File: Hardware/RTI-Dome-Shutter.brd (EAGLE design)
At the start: 80 x 71.1 mm, 42 parts, among them IC1 24AA128ST, IC5 74LVC245, IC6 74ABT245, J1 POWERPOLE_POWER45A

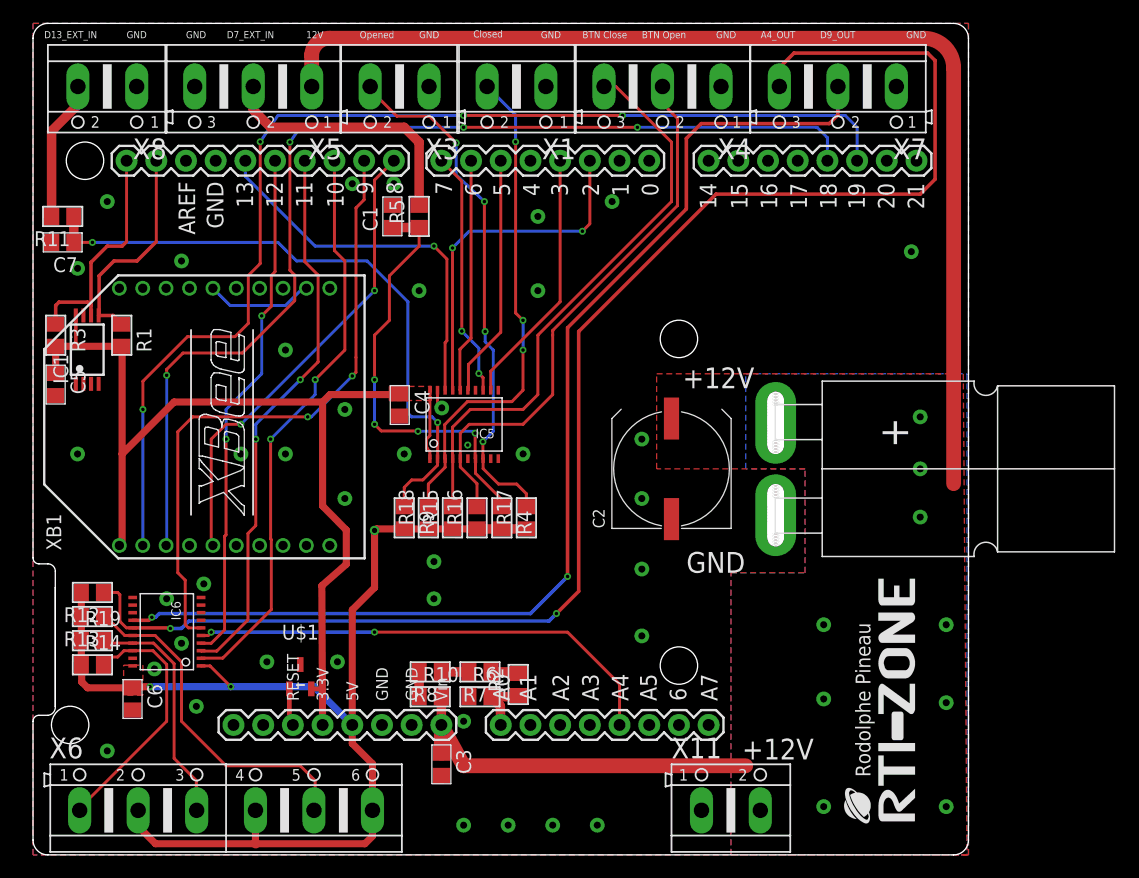
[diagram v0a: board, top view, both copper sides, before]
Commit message: Change pin mode for better interrupt detection
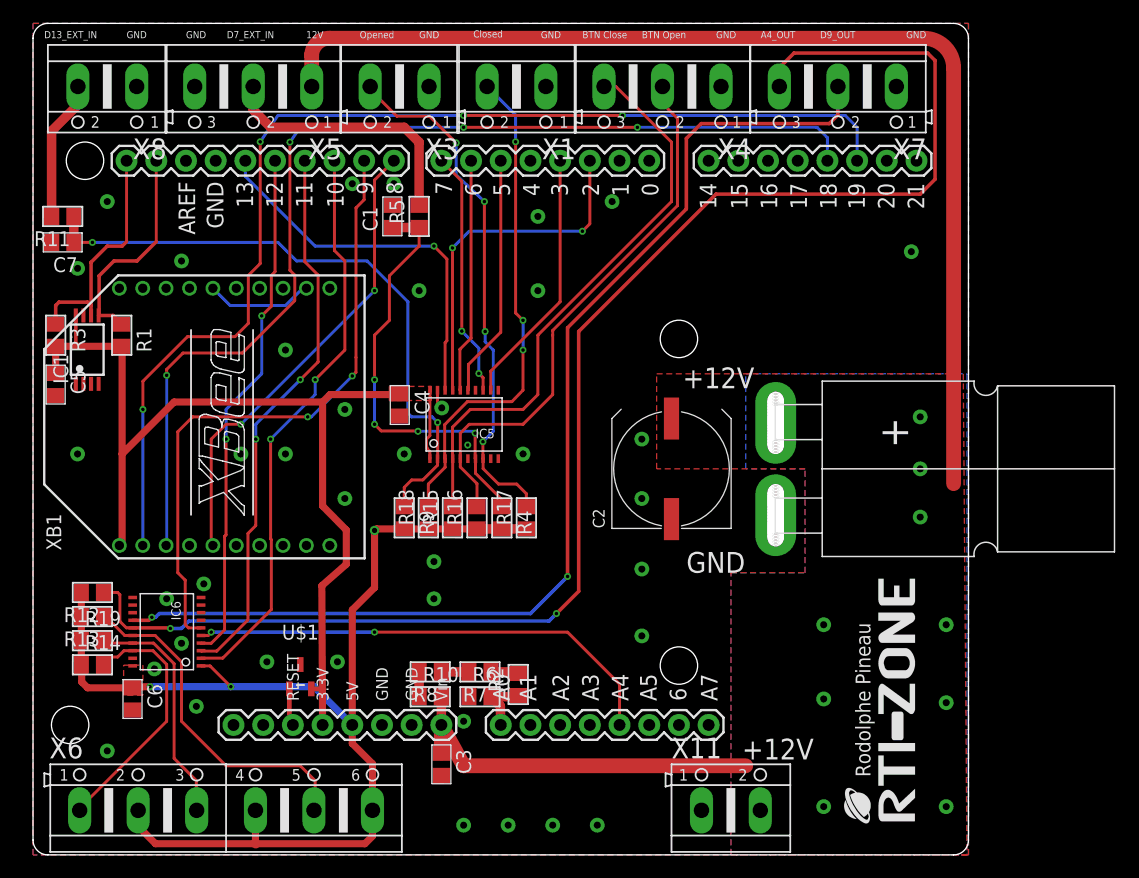
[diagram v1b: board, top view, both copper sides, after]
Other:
- outline, holes or cut-outs redrawn
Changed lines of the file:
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@@
 <setting verticaltext="up"/>
 </settings>
-<grid distance="0.3175" unitdist="mm" unit="mm" style="lines" multiple="1" display="yes" altdistance="0.03175" altunitdist="mm" altunit="mm"/>
+<grid distance="0.635" unitdist="mm" unit="mm" style="lines" multiple="1" display="yes" altdistance="0.03175" altunitdist="mm" altunit="mm"/>
 <layers>
 <layer number="1" name="Top" color="4" fill="1" visible="yes" active="yes"/>
@@
 <text x="55.88" y="24.13" size="1.778" layer="21">GND</text>
 <text x="55.5625" y="39.90975" size="1.778" layer="21">+12V</text>
-<wire x1="1.905" y1="22.86" x2="1.905" y2="12.7" width="0" layer="20"/>
 <text x="37.6555" y="69.9135" size="0.6096" layer="21">Closed</text>
 <text x="27.94" y="69.85" size="0.6096" layer="21">Opened</text>
-<wire x1="0.508" y1="11.938" x2="1.27" y2="11.938" width="0" layer="20"/>
-<wire x1="0" y1="1.27" x2="0" y2="11.43" width="0" layer="20"/>
-<wire x1="1.905" y1="12.7" x2="1.905" y2="22.86" width="0" layer="20"/>
-<wire x1="0" y1="25.4" x2="0" y2="69.85" width="0" layer="20"/>
-<wire x1="1.27" y1="71.12" x2="78.74" y2="71.12" width="0" layer="20"/>
-<wire x1="80.01" y1="69.85" x2="80.01" y2="1.27" width="0" layer="20"/>
-<wire x1="78.74" y1="0" x2="1.27" y2="0" width="0" layer="20"/>
-<wire x1="1.905" y1="12.7" x2="1.27" y2="11.938" width="0" layer="20" curve="-90"/>
-<wire x1="78.74" y1="0" x2="80.01" y2="1.27" width="0" layer="20" curve="90"/>
-<wire x1="80.01" y1="69.85" x2="78.74" y2="71.12" width="0" layer="20" curve="90"/>
-<wire x1="1.27" y1="71.12" x2="0" y2="69.85" width="0" layer="20" curve="90"/>
-<wire x1="1.27" y1="0" x2="0" y2="1.27" width="0" layer="20" curve="-90"/>
-<wire x1="1.905" y1="24.257" x2="1.905" y2="22.86" width="0" layer="20"/>
-<wire x1="0.508" y1="24.892" x2="1.27" y2="24.892" width="0" layer="20"/>
-<wire x1="1.27" y1="24.892" x2="1.905" y2="24.257" width="0" layer="20" curve="-90"/>
-<wire x1="0.508" y1="24.892" x2="0" y2="25.4" width="0" layer="20" curve="-90"/>
-<wire x1="0" y1="11.43" x2="0.508" y2="11.938" width="0" layer="20" curve="-90"/>
 <text x="16.5735" y="69.85" size="0.6096" layer="21">D7_EXT_IN</text>
 <text x="13.081" y="69.85" size="0.6096" layer="21">GND</text>
@@
 <text x="60.6425" y="8.15975" size="1.778" layer="21">+12V</text>
 <text x="62.23" y="69.85" size="0.6096" layer="21">A4_OUT</text>
+<wire x1="0" y1="1.27" x2="0" y2="69.85" width="0" layer="20"/>
+<wire x1="0" y1="69.85" x2="1.27" y2="71.12" width="0" layer="20" curve="-90"/>
+<wire x1="1.27" y1="71.12" x2="78.74" y2="71.12" width="0" layer="20"/>
+<wire x1="78.74" y1="71.12" x2="80.01" y2="69.85" width="0" layer="20" curve="-90"/>
+<wire x1="80.01" y1="69.85" x2="80.01" y2="1.27" width="0" layer="20"/>
+<wire x1="80.01" y1="1.27" x2="78.74" y2="0" width="0" layer="20" curve="-90"/>
+<wire x1="78.74" y1="0" x2="1.27" y2="0" width="0" layer="20"/>
+<wire x1="1.27" y1="0" x2="0" y2="1.27" width="0" layer="20" curve="-90"/>
 </plain>
 <attributes>

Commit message: All recent update to pcb and code are in.
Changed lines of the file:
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@@
 <text x="0.9525" y="69.85" size="0.6096" layer="21">D13_EXT_IN</text>
 <text x="6.50875" y="68.61175" size="0.6096" layer="22" rot="MR0">D13_EXT_IN</text>
-<text x="34.925" y="3.4925" size="1.778" layer="51">Dome Shutter</text>
+<text x="34.925" y="3.4925" size="1.778" layer="25">Dome Shutter</text>
 <text x="60.6425" y="8.15975" size="1.778" layer="21">+12V</text>
 <text x="62.23" y="69.85" size="0.6096" layer="21">A4_OUT</text>

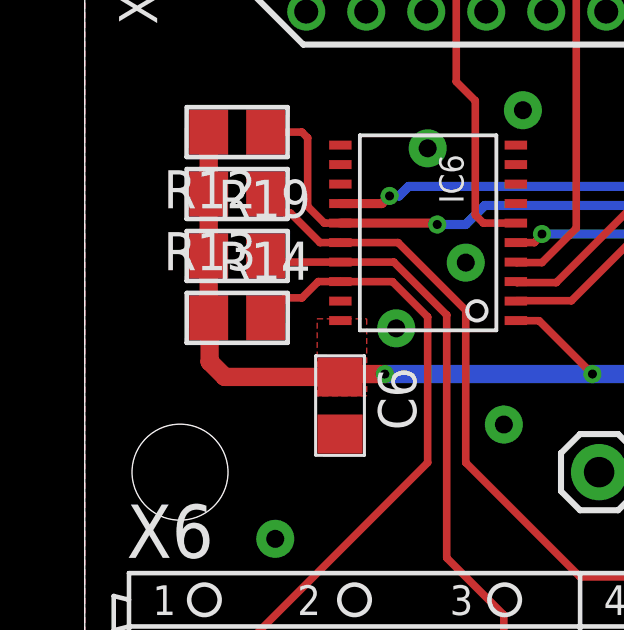
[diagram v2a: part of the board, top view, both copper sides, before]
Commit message: Re-did some of the core to receive data from network and wireless connection
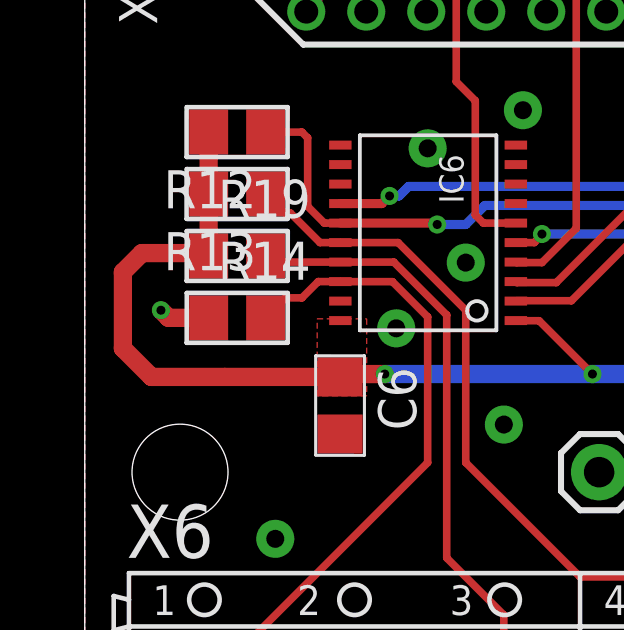
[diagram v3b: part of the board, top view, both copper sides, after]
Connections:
- net GND: now also R14.1
- net VCC: no longer R14.1
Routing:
- net VCC: track 102.0 -> 107.2 mm
- net GND: track 1.66 -> 3.36 mm, vias 39 -> 40
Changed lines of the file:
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@@
 <via x="12.7" y="18.0975" extent="1-16" drill="0.6" diameter="1.27"/>
 <contactref element="IC5" pad="P$9"/>
+<contactref element="R14" pad="1"/>
+<wire x1="4.13" y1="16.256" x2="2.794" y2="16.256" width="0.6096" layer="1"/>
+<wire x1="2.794" y1="16.256" x2="2.54" y2="16.51" width="0.6096" layer="1"/>
+<via x="2.54" y="16.51" extent="1-16" drill="0.3"/>
 </signal>
 <signal name="+12V" class="1">
@@
 <contactref element="R15" pad="1"/>
 <contactref element="R16" pad="1"/>
-<contactref element="R14" pad="1"/>
 <contactref element="R19" pad="1"/>
 <contactref element="R4" pad="2"/>
@@
 <wire x1="19.0246" y1="3.81" x2="19.0246" y2="0.9779" width="0.6096" layer="1"/>
 <wire x1="19.0246" y1="0.9779" x2="19.05" y2="0.9525" width="0.8128" layer="1"/>
-<wire x1="4.16175" y1="14.793" x2="4.66725" y2="14.2875" width="0.6096" layer="1"/>
 <wire x1="4.66725" y1="14.2875" x2="8.5065" y2="14.2875" width="0.6096" layer="1"/>
 <wire x1="8.5065" y1="14.2875" x2="8.509" y2="14.285" width="0.8128" layer="1"/>
 <contactref element="IC6" pad="P$20"/>
-<wire x1="4.16175" y1="14.793" x2="4.16175" y2="16.22425" width="0.6096" layer="1"/>
-<wire x1="4.16175" y1="16.22425" x2="4.13" y2="16.256" width="0.6096" layer="1"/>
-<wire x1="4.13" y1="16.256" x2="4.13" y2="18.31975" width="0.6096" layer="1"/>
 <wire x1="4.13" y1="20.3835" x2="3.8735" y2="20.3835" width="0.6096" layer="1"/>
 <wire x1="3.8735" y1="20.3835" x2="3.81" y2="20.32" width="0.6096" layer="1"/>
@@
 <wire x1="16.92275" y1="14.38275" x2="24.03475" y2="14.38275" width="0.6096" layer="16"/>
 <wire x1="24.03475" y1="14.38275" x2="27.305" y2="11.1125" width="0.6096" layer="16"/>
+<wire x1="4.66725" y1="14.2875" x2="2.2225" y2="14.2875" width="0.6096" layer="1"/>
+<wire x1="2.2225" y1="14.2875" x2="1.27" y2="15.24" width="0.6096" layer="1"/>
+<wire x1="1.27" y1="15.24" x2="1.27" y2="17.78" width="0.6096" layer="1"/>
+<wire x1="1.27" y1="17.78" x2="1.905" y2="18.415" width="0.6096" layer="1"/>
+<wire x1="1.905" y1="18.415" x2="4.03475" y2="18.415" width="0.6096" layer="1"/>
+<wire x1="4.03475" y1="18.415" x2="4.13" y2="18.31975" width="0.6096" layer="1"/>
 </signal>
 <signal name="N$2">

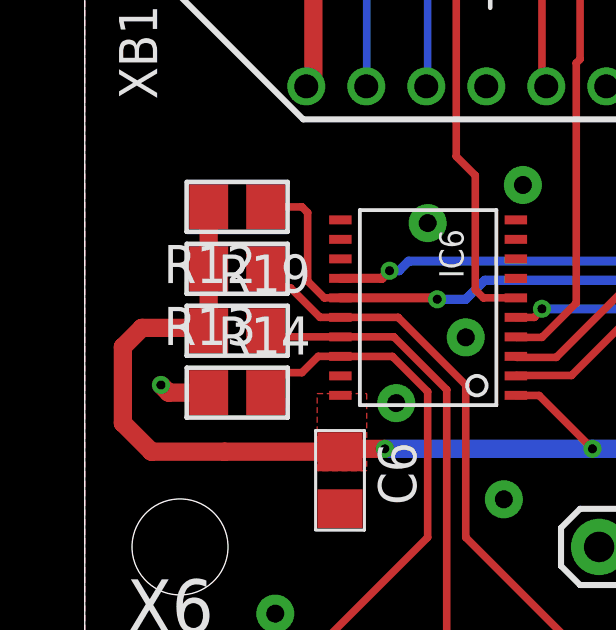
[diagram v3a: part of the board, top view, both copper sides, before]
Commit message: Making some pull-up pull-down to get a better OFF state when the controller is not powered but the stepper driver is.
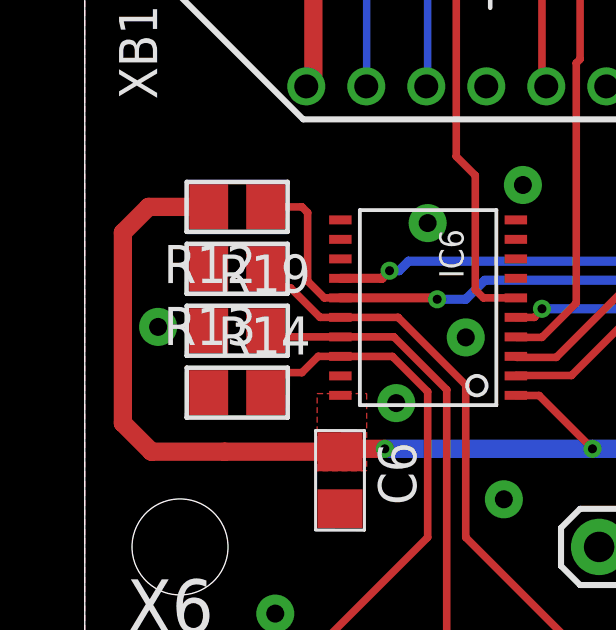
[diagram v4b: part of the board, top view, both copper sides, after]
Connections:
- net GND: now also R13.2, R19.1
- net VCC: no longer R13.2, R19.1
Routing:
- net GND: track 3.36 -> 1.66 mm
- net VCC: track 107.2 -> 106.6 mm
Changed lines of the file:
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@@
 <contactref element="IC5" pad="P$9"/>
 <contactref element="R14" pad="1"/>
-<wire x1="4.13" y1="16.256" x2="2.794" y2="16.256" width="0.6096" layer="1"/>
-<wire x1="2.794" y1="16.256" x2="2.54" y2="16.51" width="0.6096" layer="1"/>
-<via x="2.54" y="16.51" extent="1-16" drill="0.3"/>
+<contactref element="R13" pad="2"/>
+<contactref element="R19" pad="1"/>
+<via x="2.44475" y="18.44675" extent="1-16" drill="0.6" diameter="1.27"/>
 </signal>
 <signal name="+12V" class="1">
@@
 <signal name="VCC">
 <contactref element="R18" pad="1"/>
-<contactref element="R13" pad="2"/>
 <contactref element="R17" pad="1"/>
 <contactref element="R15" pad="1"/>
 <contactref element="R16" pad="1"/>
-<contactref element="R19" pad="1"/>
 <contactref element="R4" pad="2"/>
 <wire x1="27.305" y1="11.1125" x2="27.305" y2="20.955" width="0.6096" layer="1"/>
@@
 <wire x1="8.5065" y1="14.2875" x2="8.509" y2="14.285" width="0.8128" layer="1"/>
 <contactref element="IC6" pad="P$20"/>
-<wire x1="4.13" y1="20.3835" x2="3.8735" y2="20.3835" width="0.6096" layer="1"/>
-<wire x1="3.8735" y1="20.3835" x2="3.81" y2="20.32" width="0.6096" layer="1"/>
-<wire x1="4.13" y1="18.31975" x2="4.13" y2="20.3835" width="0.6096" layer="1"/>
-<wire x1="4.13" y1="20.3835" x2="4.13" y2="22.44725" width="0.6096" layer="1"/>
 <wire x1="29.398" y1="27.879" x2="29.21" y2="27.7495" width="0.6096" layer="1"/>
 <wire x1="33.81375" y1="27.879" x2="35.8775" y2="27.879" width="0.6096" layer="1"/>
@@
 <wire x1="4.66725" y1="14.2875" x2="2.2225" y2="14.2875" width="0.6096" layer="1"/>
 <wire x1="2.2225" y1="14.2875" x2="1.27" y2="15.24" width="0.6096" layer="1"/>
-<wire x1="1.27" y1="15.24" x2="1.27" y2="17.78" width="0.6096" layer="1"/>
-<wire x1="1.27" y1="17.78" x2="1.905" y2="18.415" width="0.6096" layer="1"/>
-<wire x1="1.905" y1="18.415" x2="4.03475" y2="18.415" width="0.6096" layer="1"/>
-<wire x1="4.03475" y1="18.415" x2="4.13" y2="18.31975" width="0.6096" layer="1"/>
+<wire x1="1.27" y1="15.24" x2="1.27" y2="21.59" width="0.6096" layer="1"/>
+<wire x1="4.13" y1="22.44725" x2="2.12725" y2="22.44725" width="0.6096" layer="1"/>
+<wire x1="2.12725" y1="22.44725" x2="1.27" y2="21.59" width="0.6096" layer="1"/>
 </signal>
 <signal name="N$2">

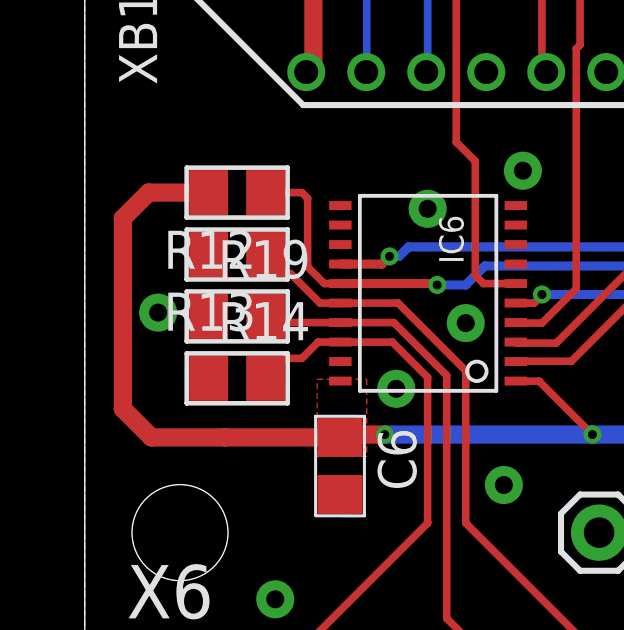
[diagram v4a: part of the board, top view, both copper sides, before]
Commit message: Pull-down doesn't really help. Setting back to pull-up to make sure enable does enable :)
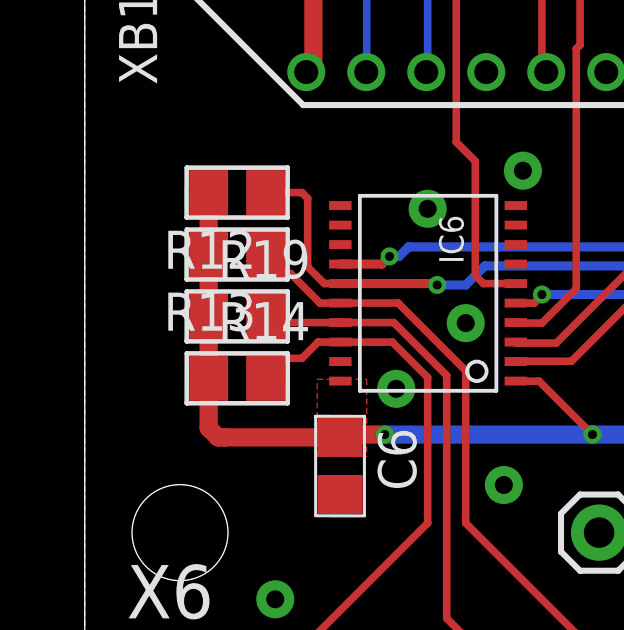
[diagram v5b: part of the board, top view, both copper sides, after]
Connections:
- net GND: no longer R13.2, R14.1, R19.1
- net VCC: now also R13.2, R14.1, R19.1
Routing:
- net VCC: track 106.6 -> 101.8 mm
- net GND: vias 40 -> 39
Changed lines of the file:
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@@
 <via x="12.7" y="18.0975" extent="1-16" drill="0.6" diameter="1.27"/>
 <contactref element="IC5" pad="P$9"/>
-<contactref element="R14" pad="1"/>
-<contactref element="R13" pad="2"/>
-<contactref element="R19" pad="1"/>
-<via x="2.44475" y="18.44675" extent="1-16" drill="0.6" diameter="1.27"/>
 </signal>
 <signal name="+12V" class="1">
@@
 <wire x1="16.92275" y1="14.38275" x2="24.03475" y2="14.38275" width="0.6096" layer="16"/>
 <wire x1="24.03475" y1="14.38275" x2="27.305" y2="11.1125" width="0.6096" layer="16"/>
-<wire x1="4.66725" y1="14.2875" x2="2.2225" y2="14.2875" width="0.6096" layer="1"/>
-<wire x1="2.2225" y1="14.2875" x2="1.27" y2="15.24" width="0.6096" layer="1"/>
-<wire x1="1.27" y1="15.24" x2="1.27" y2="21.59" width="0.6096" layer="1"/>
-<wire x1="4.13" y1="22.44725" x2="2.12725" y2="22.44725" width="0.6096" layer="1"/>
-<wire x1="2.12725" y1="22.44725" x2="1.27" y2="21.59" width="0.6096" layer="1"/>
+<wire x1="4.66725" y1="14.2875" x2="4.445" y2="14.2875" width="0.6096" layer="1"/>
+<contactref element="R14" pad="1"/>
+<contactref element="R19" pad="1"/>
+<contactref element="R13" pad="2"/>
+<wire x1="4.13" y1="16.256" x2="4.13" y2="14.6025" width="0.6096" layer="1"/>
+<wire x1="4.13" y1="14.6025" x2="4.445" y2="14.2875" width="0.6096" layer="1"/>
+<wire x1="4.13" y1="18.31975" x2="4.13" y2="16.256" width="0.6096" layer="1"/>
+<wire x1="4.13" y1="20.3835" x2="4.13" y2="18.31975" width="0.6096" layer="1"/>
+<wire x1="4.13" y1="22.44725" x2="4.13" y2="20.3835" width="0.6096" layer="1"/>
 </signal>
 <signal name="N$2">

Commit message: Fix a few component values.
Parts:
- R1, R3: value 1K -> 2.2K
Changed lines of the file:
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@@
 <attribute name="OC_FARNELL" value="unknown" x="-2.9845" y="55.91175" size="1.778" layer="27" display="off"/>
 </element>
-<element name="R1" library="rti" package="R0805" value="1K" x="7.58825" y="44.45" rot="R270"/>
-<element name="R3" library="rti" package="R0805" value="1K" x="1.93675" y="44.45" rot="R270"/>
+<element name="R1" library="rti" package="R0805" value="2.2K" x="7.58825" y="44.45" rot="R270"/>
+<element name="R3" library="rti" package="R0805" value="2.2K" x="1.93675" y="44.45" rot="R270"/>
 <element name="C5" library="rti" package="C0805" value="100nF" x="1.93675" y="40.22725" rot="R270"/>
 <element name="C6" library="rti" package="C0805" value="100nF" x="8.509" y="13.335" rot="R270"/>
